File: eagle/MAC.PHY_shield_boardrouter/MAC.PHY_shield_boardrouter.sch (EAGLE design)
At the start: 21 parts, among them IC1 ENC28J60SP, Q1 CSM-7X-DU

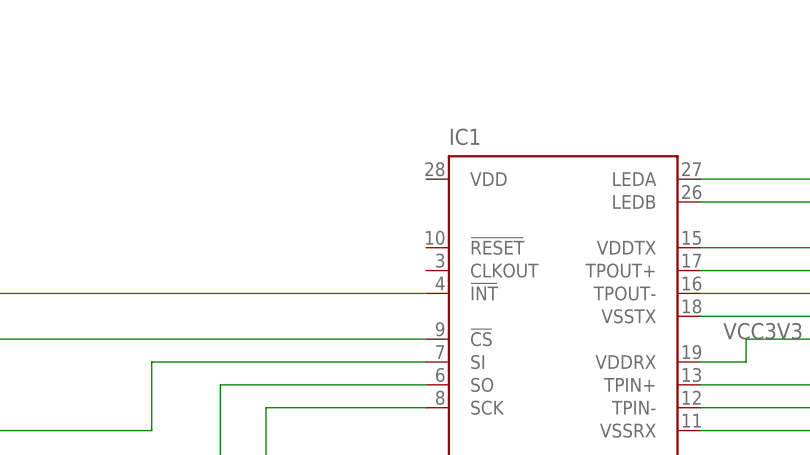
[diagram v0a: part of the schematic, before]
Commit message: Finished the PDIP dev board for the enc28J60
Signed-off-by: Pavlo Manovi <pavlo.manovi@gmail.com>
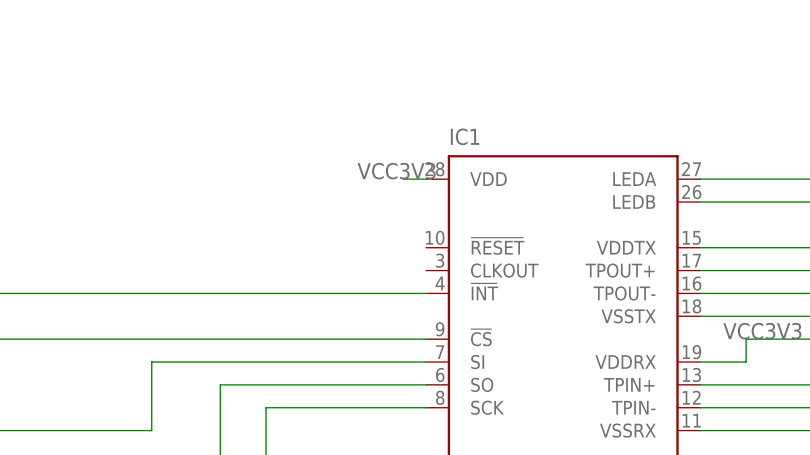
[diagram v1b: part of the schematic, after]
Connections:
- net VCC3V3: now also IC1.VDD
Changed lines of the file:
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@@
 <pinref part="IC1" gate="G$1" pin="VDDPLL"/>
+</segment>
+<segment>
+<pinref part="IC1" gate="G$1" pin="VDD"/>
+<wire x1="53.34" y1="68.58" x2="50.8" y2="68.58" width="0.2032" layer="91"/>
+<label x="45.72" y="68.58" size="1.778" layer="95"/>
 </segment>
 </net>
